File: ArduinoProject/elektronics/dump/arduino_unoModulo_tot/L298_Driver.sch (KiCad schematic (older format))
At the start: 6 parts, among them U1 L298D, U3 74AHC1G04, U4 74AHC1G04

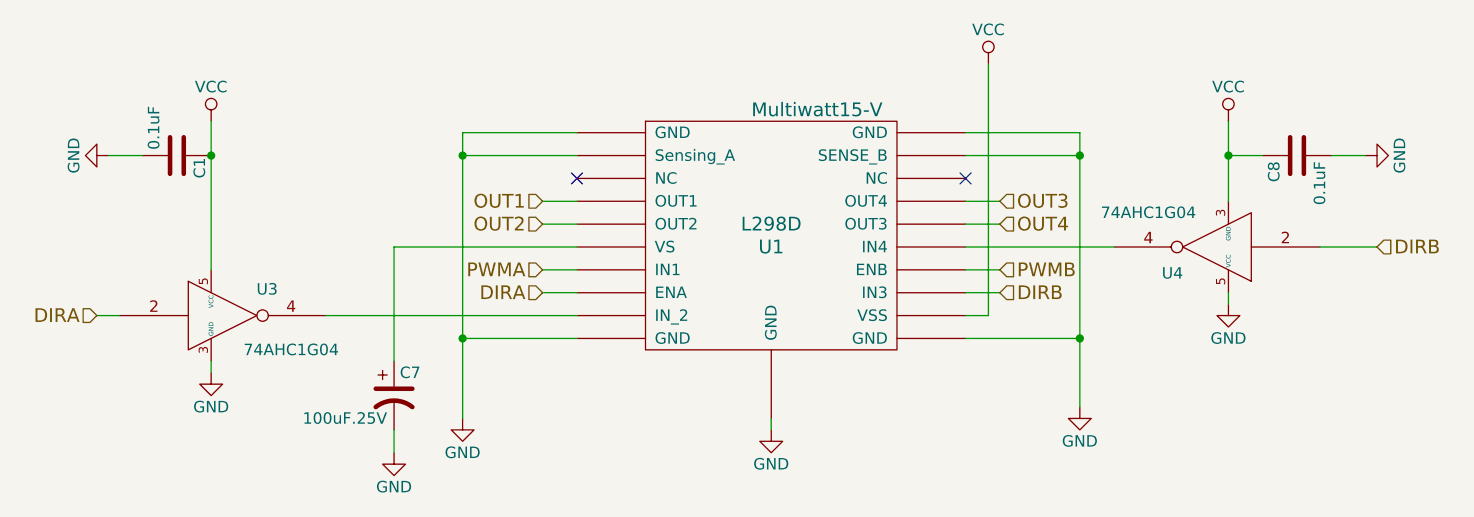
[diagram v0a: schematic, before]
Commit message: kicad schema altered: alles op 1 PCB
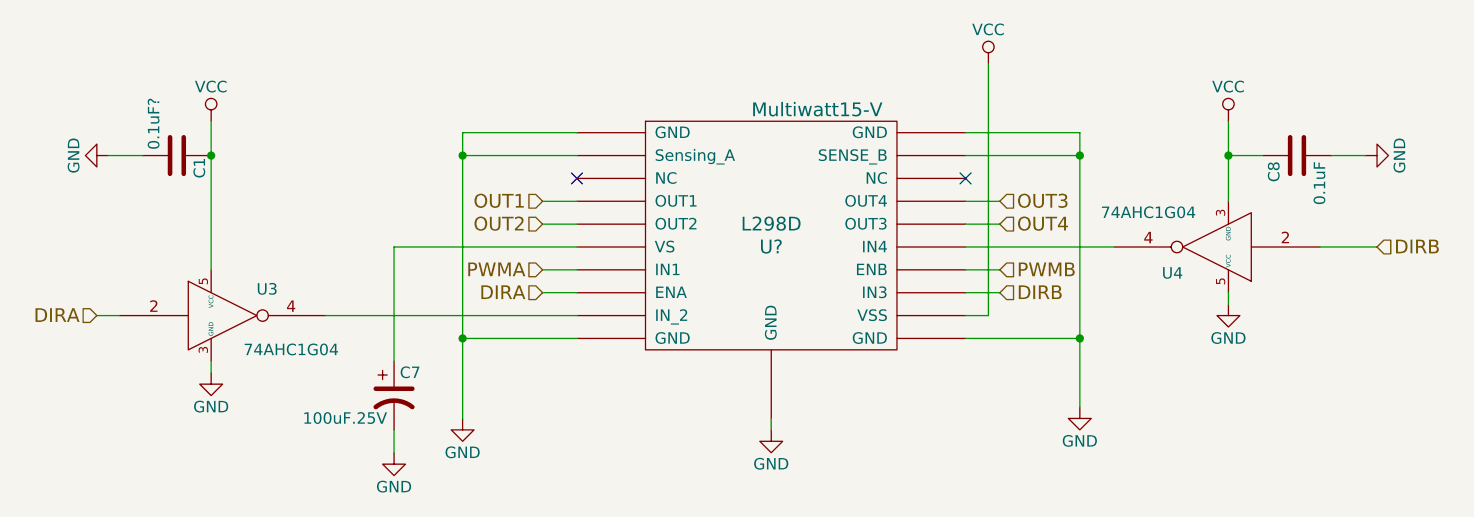
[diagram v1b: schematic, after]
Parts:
- renumbered 0.1uF to 0.1uF?, U1 to U?
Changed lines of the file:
@@
 $Descr A4 11693 8268
 encoding utf-8
-Sheet 4 6
+Sheet 6 8
 Title ""
 Date ""
@@
 $EndDescr
 $Comp
-L L298D U1
+L L298D U?
 U 1 1 5A8D786D
 P 5800 3000
-F 0 "U1" H 5800 3000 60  0000 C CNN
+F 0 "U?" H 5800 3000 60  0000 C CNN
 F 1 "L298D" H 5800 3100 60  0000 C CNN
 F 2 "Multiwatt15-V" H 6000 3600 60  0000 C CNN
@@
 	7150 3400 6650 3400
 $Comp
-L GND #PWR013
+L GND #PWR?
 U 1 1 5A8D786E
 P 7150 3700
-F 0 "#PWR013" H 7150 3450 50  0001 C CNN
+F 0 "#PWR?" H 7150 3450 50  0001 C CNN
 F 1 "GND" H 7150 3550 50  0000 C CNN
 F 2 "" H 7150 3700 50  0001 C CNN
@@
 $EndComp
 $Comp
-L GND #PWR014
+L GND #PWR?
 U 1 1 5A8D786F
 P 5800 3800
-F 0 "#PWR014" H 5800 3550 50  0001 C CNN
+F 0 "#PWR?" H 5800 3550 50  0001 C CNN
 F 1 "GND" H 5800 3650 50  0000 C CNN
 F 2 "" H 5800 3800 50  0001 C CNN
@@
 $EndComp
 $Comp
-L GND #PWR015
+L GND #PWR?
 U 1 1 5A8D7870
 P 4450 3750
-F 0 "#PWR015" H 4450 3500 50  0001 C CNN
+F 0 "#PWR?" H 4450 3500 50  0001 C CNN
 F 1 "GND" H 4450 3600 50  0000 C CNN
 F 2 "" H 4450 3750 50  0001 C CNN
@@
 	2850 3300 2950 3300
 $Comp
-L GND #PWR016
+L GND #PWR?
 U 1 1 5A8D7873
 P 7800 3250
-F 0 "#PWR016" H 7800 3000 50  0001 C CNN
+F 0 "#PWR?" H 7800 3000 50  0001 C CNN
 F 1 "GND" H 7800 3100 50  0000 C CNN
 F 2 "" H 7800 3250 50  0001 C CNN
@@
 $EndComp
 $Comp
-L GND #PWR017
+L GND #PWR?
 U 1 1 5A8D7874
 P 3350 3550
-F 0 "#PWR017" H 3350 3300 50  0001 C CNN
+F 0 "#PWR?" H 3350 3300 50  0001 C CNN
 F 1 "GND" H 3350 3400 50  0000 C CNN
 F 2 "" H 3350 3550 50  0001 C CNN
@@
 	7800 3250 7800 3200
 $Comp
-L VCC #PWR018
+L VCC #PWR?
 U 1 1 5A8D7875
 P 7800 2450
-F 0 "#PWR018" H 7800 2300 50  0001 C CNN
+F 0 "#PWR?" H 7800 2300 50  0001 C CNN
 F 1 "VCC" H 7800 2600 50  0000 C CNN
 F 2 "" H 7800 2450 50  0001 C CNN
@@
 $EndComp
 $Comp
-L VCC #PWR019
+L VCC #PWR?
 U 1 1 5A8D7876
 P 3350 2450
-F 0 "#PWR019" H 3350 2300 50  0001 C CNN
+F 0 "#PWR?" H 3350 2300 50  0001 C CNN
 F 1 "VCC" H 3350 2600 50  0000 C CNN
 F 2 "" H 3350 2450 50  0001 C CNN
@@
 $EndComp
 $Comp
-L GND #PWR020
+L GND #PWR?
 U 1 1 5A964733
 P 8400 2600
-F 0 "#PWR020" H 8400 2350 50  0001 C CNN
+F 0 "#PWR?" H 8400 2350 50  0001 C CNN
 F 1 "GND" H 8400 2450 50  0000 C CNN
 F 2 "" H 8400 2600 50  0001 C CNN
@@
 $EndComp
 $Comp
-L C 0.1uF
+L C 0.1uF?
 U 1 1 5A9647F3
 P 3200 2600
-F 0 "0.1uF" H 3225 2700 50  0000 L CNN
+F 0 "0.1uF?" H 3225 2700 50  0000 L CNN
 F 1 "C1" H 3100 2500 50  0000 L CNN
 F 2 "" H 3238 2450 50  0001 C CNN
@@
 Connection ~ 3350 2600
 $Comp
-L GND #PWR021
+L GND #PWR?
 U 1 1 5A964A96
 P 2900 2600
-F 0 "#PWR021" H 2900 2350 50  0001 C CNN
+F 0 "#PWR?" H 2900 2350 50  0001 C CNN
 F 1 "GND" H 2900 2450 50  0000 C CNN
 F 2 "" H 2900 2600 50  0001 C CNN
@@
 $EndComp
 $Comp
-L GND #PWR022
+L GND #PWR?
 U 1 1 5A964BF3
 P 4150 3900
-F 0 "#PWR022" H 4150 3650 50  0001 C CNN
+F 0 "#PWR?" H 4150 3650 50  0001 C CNN
 F 1 "GND" H 4150 3750 50  0000 C CNN
 F 2 "" H 4150 3900 50  0001 C CNN
@@
 	6750 3300 6750 2200
 $Comp
-L VCC #PWR023
+L VCC #PWR?
 U 1 1 5A964E67
 P 6750 2200
-F 0 "#PWR023" H 6750 2050 50  0001 C CNN
+F 0 "#PWR?" H 6750 2050 50  0001 C CNN
 F 1 "VCC" H 6750 2350 50  0000 C CNN
 F 2 "" H 6750 2200 50  0001 C CNN
